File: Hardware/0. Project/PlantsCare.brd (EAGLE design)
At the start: 30 x 200 mm, 22 parts, among them J1 ICSP, Q1 32.768 kHz, U1 MSP430FR4133

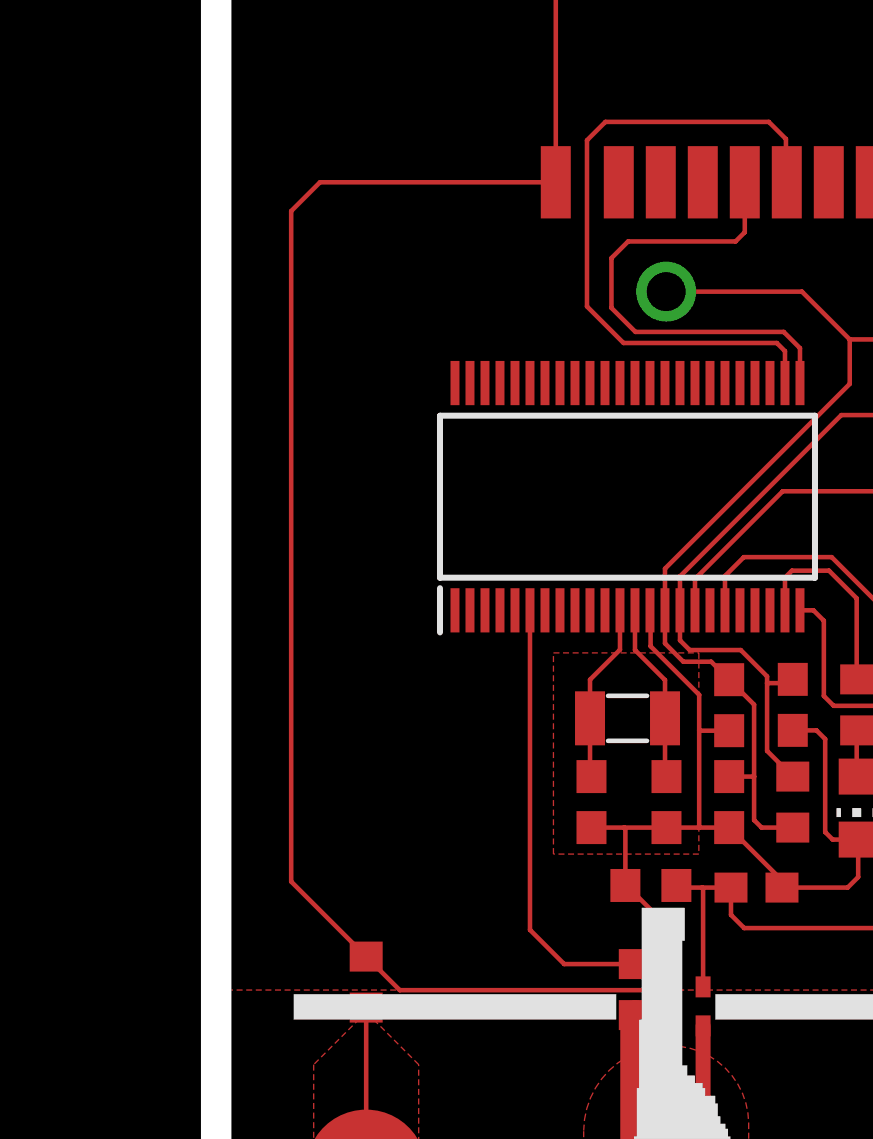
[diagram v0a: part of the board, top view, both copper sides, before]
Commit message: Project name changed to 'PlantsCare'
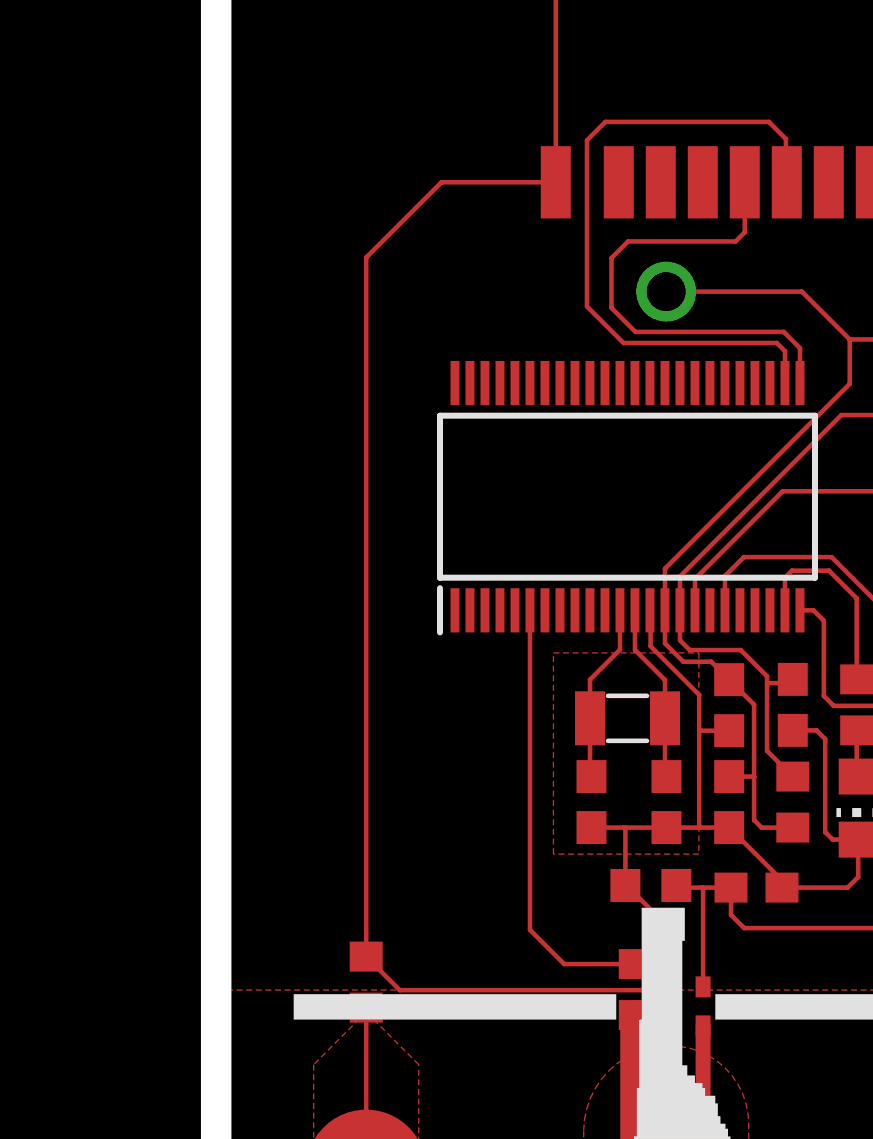
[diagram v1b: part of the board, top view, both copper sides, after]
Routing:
- net GND: track 179.8 -> 175.3 mm
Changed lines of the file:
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@@
 <setting verticaltext="up"/>
 </settings>
-<grid distance="0.003333" unitdist="inch" unit="inch" style="lines" multiple="1" display="yes" altdistance="5" altunitdist="mil" altunit="mm"/>
+<grid distance="0.01" unitdist="mm" unit="mm" style="lines" multiple="1" display="yes" altdistance="5" altunitdist="mil" altunit="mm"/>
 <layers>
 <layer number="1" name="Top" color="4" fill="1" visible="yes" active="yes"/>
@@
 <wire x1="11.32" y1="183.2" x2="11.32" y2="173.66" width="0.1524" layer="1"/>
 <wire x1="14.82" y1="183.2" x2="11.32" y2="183.2" width="0.1524" layer="1"/>
-<wire x1="11.32" y1="173.66" x2="3.46" y2="173.66" width="0.1524" layer="1"/>
-<wire x1="3.46" y1="173.66" x2="2.5" y2="172.7" width="0.1524" layer="1"/>
-<wire x1="2.5" y1="172.7" x2="2.5" y2="150.35" width="0.1524" layer="1"/>
-<wire x1="2.5" y1="150.35" x2="5" y2="147.85" width="0.1524" layer="1"/>
+<wire x1="7.51" y1="173.66" x2="11.32" y2="173.66" width="0.1524" layer="1"/>
 <wire x1="28.3998" y1="152.7098" x2="27.46" y2="151.77" width="0.1524" layer="1"/>
 <wire x1="27.46" y1="151.77" x2="25.56" y2="151.77" width="0.1524" layer="1"/>
@@
 <wire x1="6.1198" y1="146.7302" x2="5" y2="147.85" width="0.1524" layer="1"/>
 <wire x1="14.8302" y1="146.7302" x2="6.1198" y2="146.7302" width="0.1524" layer="1"/>
+<wire x1="5" y1="147.85" x2="5" y2="171.15" width="0.1524" layer="1"/>
+<wire x1="5" y1="171.15" x2="7.51" y2="173.66" width="0.1524" layer="1"/>
 </signal>
 <signal name="BLE_RX">

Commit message: BOM .csv file formatted as GitHub needed
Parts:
- renumbered J1 to CN1
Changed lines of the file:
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@@
 <attribute name="VALUE" x="14.325" y="146.875" size="1.27" layer="27" rot="R270" display="off"/>
 </element>
-<element name="J1" library="con-molex" library_urn="urn:adsk.eagle:library:165" package="7395-04" package3d_urn="urn:adsk.eagle:package:8078648/1" value="ICSP" x="23.69" y="164.63" smashed="yes" rot="R90">
+<element name="CN1" library="con-molex" library_urn="urn:adsk.eagle:library:165" package="7395-04" package3d_urn="urn:adsk.eagle:package:8078648/1" value="ICSP" x="23.69" y="164.63" smashed="yes" rot="R90">
 <attribute name="MF" value="MOLEX" x="37.66" y="201.46" size="1.778" layer="27" rot="R90" display="off"/>
 <attribute name="MPN" value="" x="37.66" y="201.46" size="1.778" layer="27" rot="R90" display="off"/>
@@
 <contactref element="C3" pad="2"/>
 <contactref element="S1" pad="1"/>
-<contactref element="J1" pad="4"/>
+<contactref element="CN1" pad="4"/>
 <contactref element="BT1" pad="1"/>
 <contactref element="R6" pad="2"/>
@@
 <contactref element="R2" pad="1"/>
 <contactref element="C3" pad="1"/>
-<contactref element="J1" pad="1"/>
+<contactref element="CN1" pad="1"/>
 <contactref element="BT1" pad="2"/>
 <wire x1="14.96" y1="158.29" x2="14.96" y2="159.392" width="0.1524" layer="1"/>
@@
 <contactref element="R2" pad="2"/>
 <contactref element="U1" pad="16"/>
-<contactref element="J1" pad="2"/>
+<contactref element="CN1" pad="2"/>
 <wire x1="15.46" y1="159.392" x2="15.46" y2="158.3912125" width="0.1524" layer="1"/>
 <wire x1="20.837" y1="165.9" x2="23.69" y2="165.9" width="0.1524" layer="1"/>
@@
 <signal name="SBWTCK">
 <contactref element="U1" pad="17"/>
-<contactref element="J1" pad="3"/>
+<contactref element="CN1" pad="3"/>
 <wire x1="15.96" y1="160.437" x2="15.96" y2="159.392" width="0.1524" layer="1"/>
 <wire x1="23.69" y1="163.36" x2="18.883" y2="163.36" width="0.1524" layer="1"/>

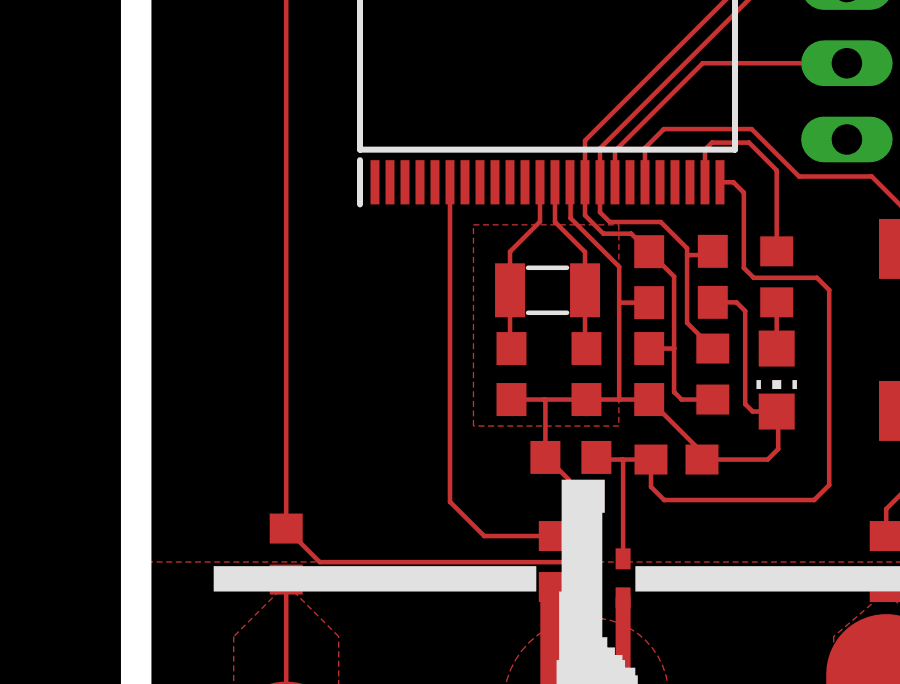
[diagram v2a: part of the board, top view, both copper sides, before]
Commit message: PCB layout needs to be updated to 1.2
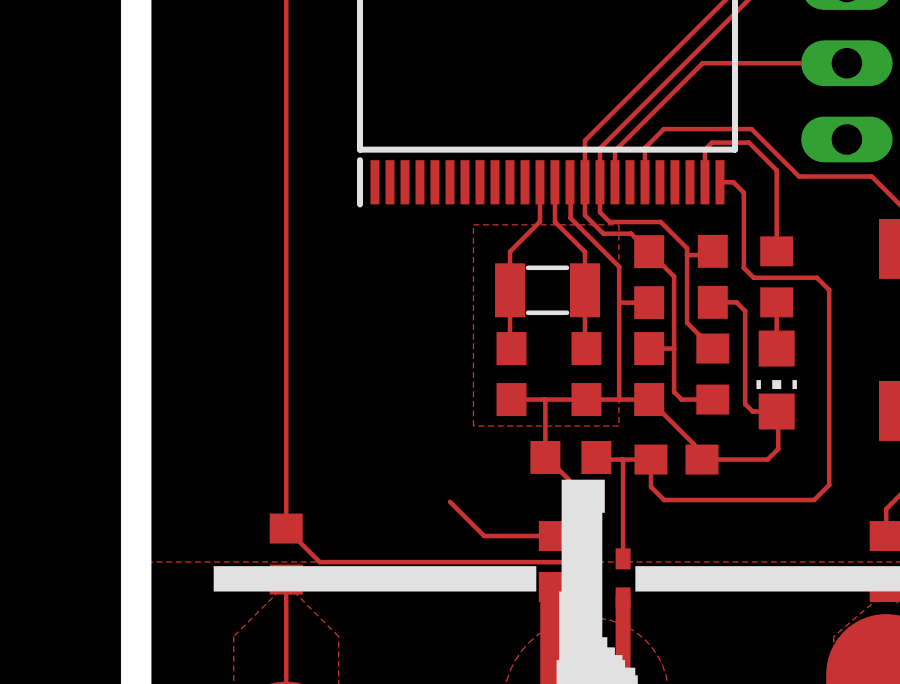
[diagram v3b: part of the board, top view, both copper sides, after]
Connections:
- removed net BLE_WAKE1: PCB1.24, R1.2
- new net BLE_STATUS: PCB1.16, U1.20
- new net BLE_WAKE: PCB1.24, R1.2, U1.21
- net HF_SQUAREWAVE: now also U1.22; no longer U1.6
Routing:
- net BLE_WAKE1: track 12.0 -> 0.00 mm
- net BLE_WAKE: track 0.00 -> 12.0 mm
- net HF_SQUAREWAVE: track 14.6 -> 3.98 mm
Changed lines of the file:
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@@
 <signal name="HF_SQUAREWAVE">
 <contactref element="R3" pad="2"/>
-<contactref element="U1" pad="6"/>
 <wire x1="13.97" y1="147.6" x2="11.6" y2="147.6" width="0.1524" layer="1"/>
-<wire x1="10.46" y1="148.74" x2="10.46" y2="159.392" width="0.1524" layer="1"/>
 <wire x1="11.6" y1="147.6" x2="10.46" y2="148.74" width="0.1524" layer="1"/>
+<contactref element="U1" pad="22"/>
+<wire x1="13.97" y1="147.6" x2="18.46" y2="159.392" width="0" layer="19" extent="1-1"/>
 </signal>
 <signal name="GND" class="2">
@@
 <wire x1="17.313" y1="171.688" x2="17.62" y2="171.995" width="0.1524" layer="1"/>
 </signal>
-<signal name="BLE_WAKE1">
+<signal name="BLE_WAKE">
 <contactref element="PCB1" pad="24"/>
 <contactref element="R1" pad="2"/>
@@
 <wire x1="13.42" y1="191.028" x2="13.42" y2="186.76" width="0.1524" layer="1"/>
 <wire x1="19.14" y1="190.944" x2="18.358" y2="191.726" width="0.1524" layer="1"/>
+<contactref element="U1" pad="21"/>
+<wire x1="17.96" y1="159.392" x2="13.42" y2="186.76" width="0" layer="19" extent="1-1"/>
 </signal>
 <signal name="3V">
@@
 <wire x1="13.97" y1="137.74" x2="15" y2="136.46" width="0.508" layer="1"/>
 </signal>
+<signal name="BLE_STATUS">
+<contactref element="PCB1" pad="16"/>
+<contactref element="U1" pad="20"/>
+<wire x1="17.46" y1="159.392" x2="25.44" y2="183.71" width="0" layer="19" extent="1-1"/>
+</signal>
 </signals>

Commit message: Minor improvemets
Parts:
- R3: value 10k -> 100k
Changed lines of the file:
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@@
 <attribute name="VALUE" x="21.125" y="152.365" size="1.27" layer="27" rot="R90" display="off"/>
 </element>
-<element name="R3" library="rcl" library_urn="urn:adsk.eagle:library:334" package="R0603" package3d_urn="urn:adsk.eagle:package:23555/3" value="10k" x="13.97" y="146.75" smashed="yes" rot="R90">
+<element name="R3" library="rcl" library_urn="urn:adsk.eagle:library:334" package="R0603" package3d_urn="urn:adsk.eagle:package:23555/3" value="100k" x="13.97" y="146.75" smashed="yes" rot="R90">
 <attribute name="NAME" x="13.335" y="146.115" size="1.27" layer="25" rot="R90" display="off"/>
 <attribute name="SPICEPREFIX" value="R" x="63.5" y="183.58" size="1.778" layer="27" rot="R90" display="off"/>
